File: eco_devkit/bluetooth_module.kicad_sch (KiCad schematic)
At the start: 0 parts

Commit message: Add bg22 symbol library and update symbol library table
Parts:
- added C1, C10, C12, C4, C6: 100nF, symbol Device:C
- added C11, C2, C3, C5: 1µF, symbol Device:C
- added C13: 1.3 pF, symbol Device:C
- added C14: 18 pF, symbol Device:C
- added C7: 1.2 pF, symbol Device:C
- added C8, C9: C, symbol Device:C
- added CDECOUPLE: 10µF, symbol Device:C
- added J1: Conn_Coaxial, symbol Connector:Conn_Coaxial
- added L1, L2: 47nH, symbol Device:L
- added L3: 2.6 nH, symbol Device:L
- added U1: ~, symbol bg22:bg22
- added Y1: 38.4 MHz, symbol Device:Crystal
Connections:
- new net: C10.1, C9.1, L1.1, U1.10 (RFVDD)
- new net: C13.1, C14.1, L3.2
- new net: C14.2, J1.1 (In)
- new net: C11.1, C12.1, L2.1, U1.13 (PAVDD)
- new net: CDECOUPLE.1, U1.24 (DECOUPLE)
- new net: C7.1, L3.1, U1.12 (RF2G4_IO)
- new net: U1.7 (HFXTAL_I), Y1.1
- new net: U1.8 (HFXTAL_O), Y1.2
- new net +3.3V: C1.1, C1.2, C10.2, C11.2, C12.2, C13.2, C2.1, C2.2, C3.1, C3.2, C4.1, C4.2, C5.1, C5.2, C6.1, C6.2, C7.2, C8.1, C8.2, C9.2, CDECOUPLE.2, J1.2 (Ext), L1.2, L2.2, U1.26 (VREGVDD), U1.27 (VREGVSS), U1.28 (DVDD), U1.29 (AVDD), U1.30 (IOVDD)
- no-connect marks 0 -> 1

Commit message: att mpn e fotoprint da bg22
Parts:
- U1: footprint (none) -> EFR32BG22C224F512GN32-C
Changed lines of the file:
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@@
 			)
 		)
-		(property "Footprint" ""
+		(property "Footprint" "EFR32BG22C224F512GN32-C"
 			(at 78.74 72.39 0)
 			(effects
@@
 			)
 		)
-		(property "Datasheet" ""
+		(property "Datasheet" "https://www.digikey.com.br/pt/products/detail/silicon-labs/EFR32BG22C224F512GN32-C/11610897"
 			(at 78.74 72.39 0)
 			(effects
@@
 			)
 		)
-		(property "Description" ""
+		(property "Description" "IC RF TXRX+MCU BLE 32QFN"
 			(at 78.74 72.39 0)
 			(effects

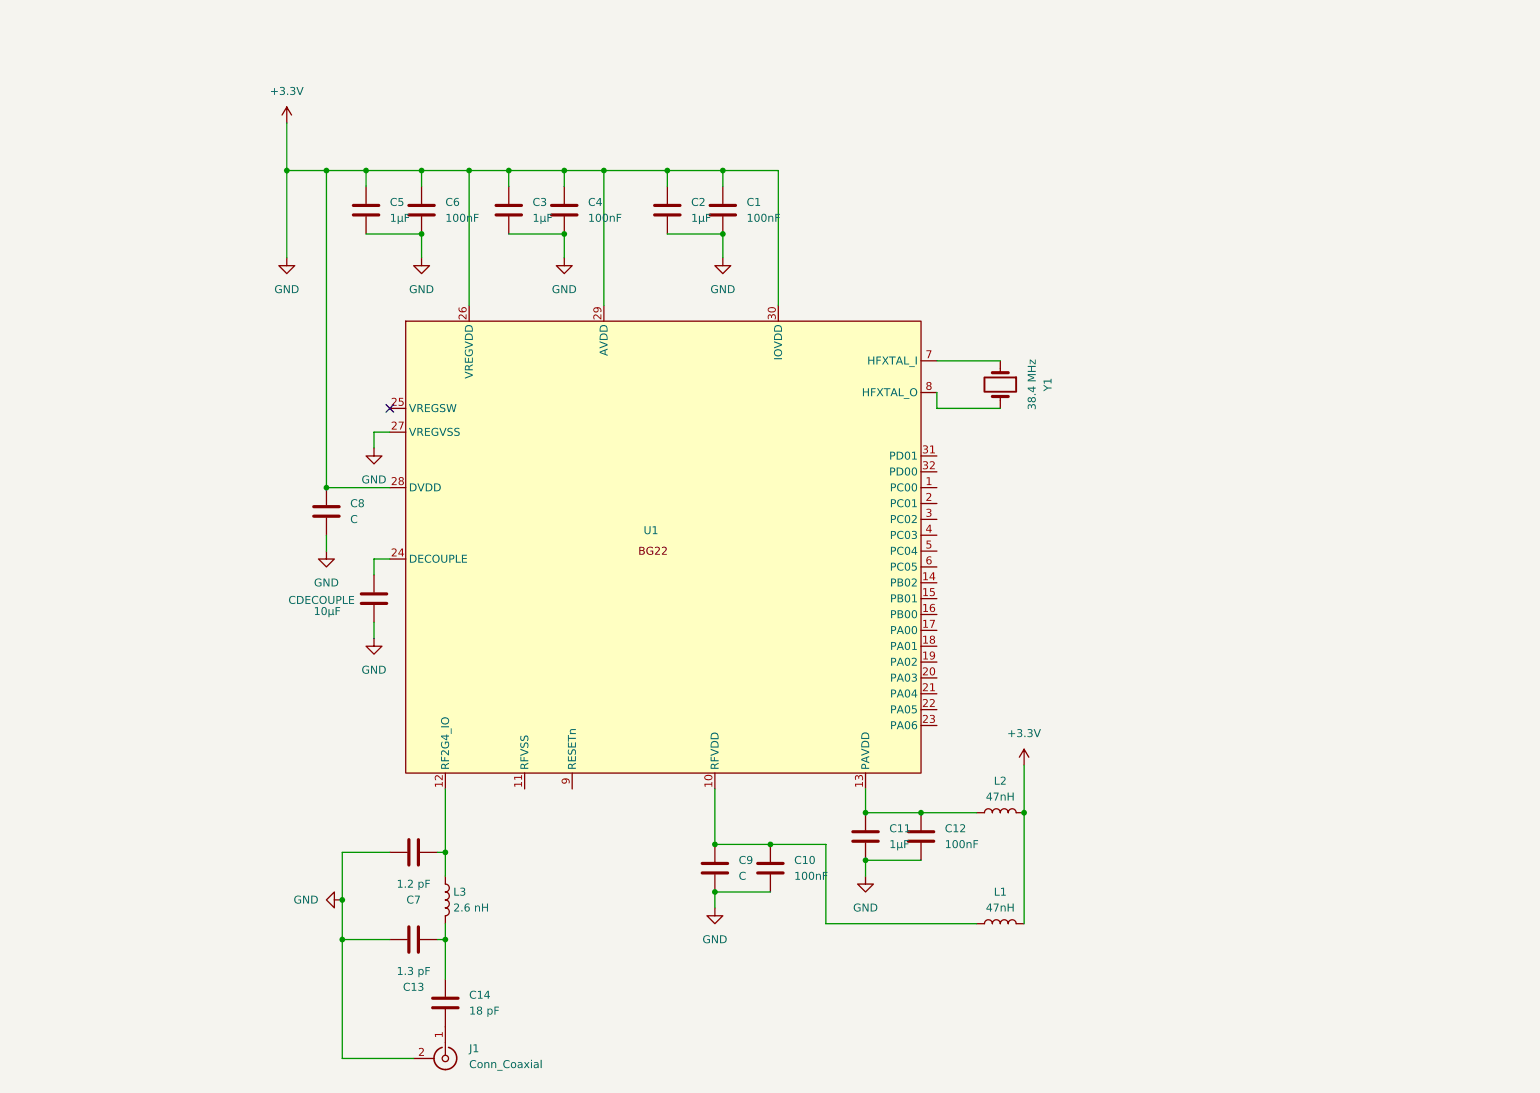
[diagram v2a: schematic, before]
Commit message: chore: ajustes nos periféricos GPIO e mapeamento do conector SWD
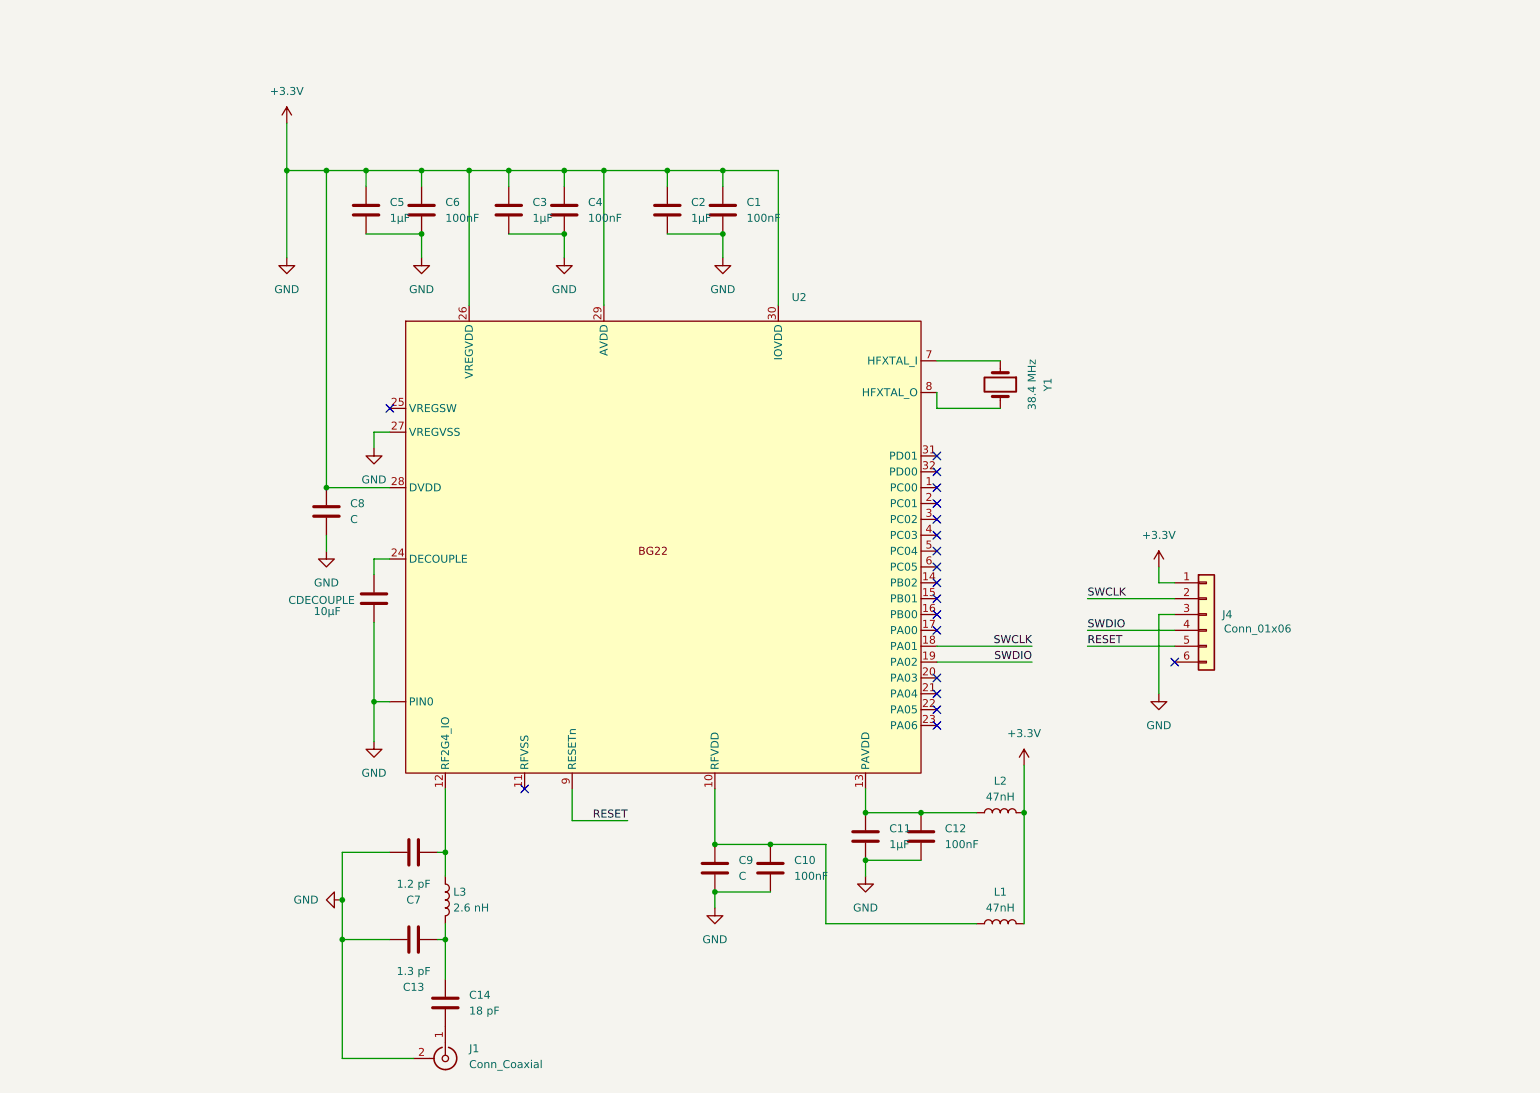
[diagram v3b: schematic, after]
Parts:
- removed U1: ~, EFR32BG22C224F512GN32-C, symbol bg22:bg22
- added J4: Conn_01x06, symbol Connector_Generic:Conn_01x06
- added U2: ~, EFR32BG22C224F512GN32-C, symbol bg22:bg22
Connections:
- net +3.3V: now also J4.1 (Pin_1), J4.3 (Pin_3), U2. (PIN0), U2.26 (VREGVDD), U2.27 (VREGVSS), U2.28 (DVDD), U2.29 (AVDD), U2.30 (IOVDD)
- net at C10.1, C9.1, L1.1: now also U2.10 (RFVDD)
- net at C11.1, C12.1, L2.1: now also U2.13 (PAVDD)
- net at CDECOUPLE.1: now also U2.24 (DECOUPLE)
- net at C7.1, L3.1: now also U2.12 (RF2G4_IO)
- net at Y1.1: now also U2.7 (HFXTAL_I)
- net at Y1.2: now also U2.8 (HFXTAL_O)
- new net RESET: J4.5 (Pin_5), U2.9 (RESETn)
- new net SWCLK: J4.2 (Pin_2), U2.18 (PA01)
- new net SWDIO: J4.4 (Pin_4), U2.19 (PA02)
- no-connect marks 1 -> 19

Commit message: Add bluetooth.
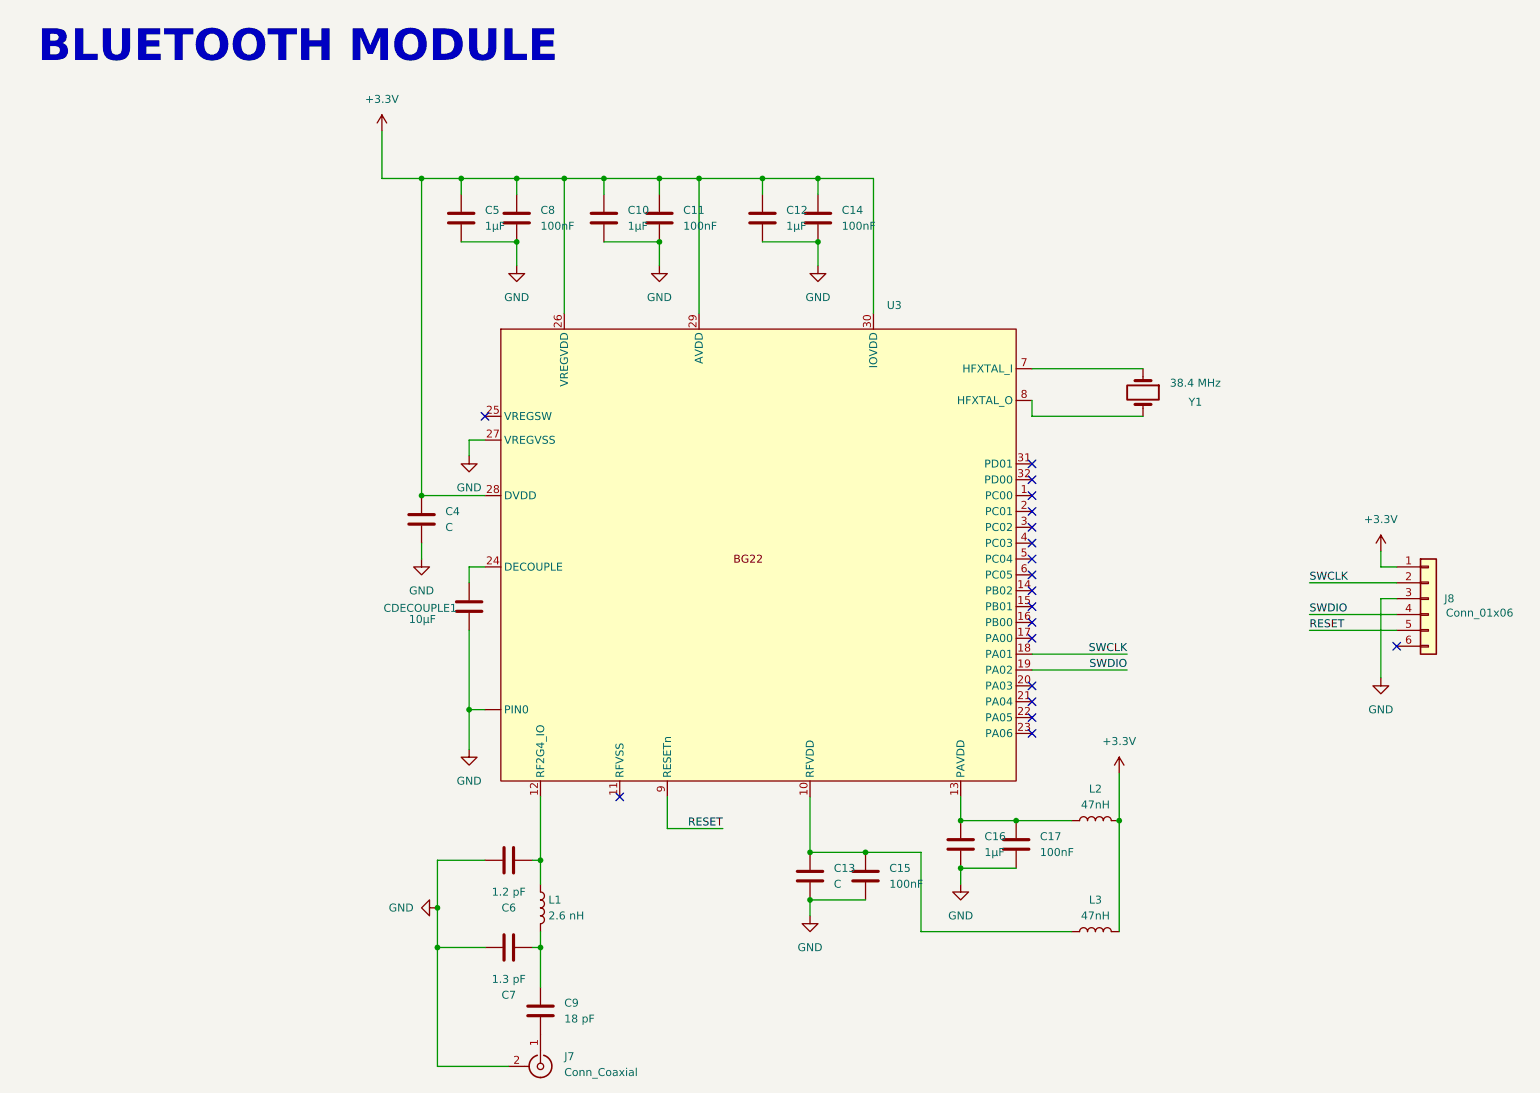
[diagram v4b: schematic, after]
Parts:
- J8: renamed from J4; footprint (none) -> Connector_PinHeader_2.54mm:PinHeader_1x06_P2.54mm_Vertical
- U3: renamed from U2; MPN (none) -> EFR32BG22C224F512GN32-C
- renumbered C3 to C10, C4 to C11, C2 to C12, C9 to C13, C1 to C14, C10 to C15, C11 to C16, C12 to C17, C8 to C4, C7 to C6, C13 to C7, C6 to C8, C14 to C9, CDECOUPLE to CDECOUPLE1, J1 to J7, L3 to L1, L1 to L3
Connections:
- net +3.3V: no longer C10.2, C11.2, C12.2, C13.2, C14.2, C15.2, C16.2, C17.2, C4.2, C5.2, C6.2, C7.2, C8.2, CDECOUPLE1.2, J7.2 (Ext), J8.3 (Pin_3), U3. (PIN0), U3.27 (VREGVSS)
- new net GND: C10.2, C11.2, C12.2, C13.2, C14.2, C15.2, C16.2, C17.2, C4.2, C5.2, C6.2, C7.2, C8.2, CDECOUPLE1.2, J7.2 (Ext), J8.3 (Pin_3), U3. (PIN0), U3.27 (VREGVSS)
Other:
- note added: "BLUETOOTH MODULE"
- moved on the sheet: C10, C11, C12, C13, C14, C15, C16, C17, C4, C5, C6, C7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

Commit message: First interation.
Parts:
- C25: renamed from C4; footprint (none) -> Capacitor_SMD:C_0402_1005Metric
- C26: renamed from C5; footprint (none) -> Capacitor_SMD:C_0402_1005Metric
- C27: renamed from C6; footprint (none) -> Capacitor_SMD:C_0402_1005Metric
- C28: renamed from C7; footprint (none) -> Capacitor_SMD:C_0402_1005Metric
- C29: renamed from C8; footprint (none) -> Capacitor_SMD:C_0402_1005Metric
- C30: renamed from C9; footprint (none) -> Capacitor_SMD:C_0402_1005Metric
- C31: renamed from C10; footprint (none) -> Capacitor_SMD:C_0402_1005Metric
- C32: renamed from C11; footprint (none) -> Capacitor_SMD:C_0402_1005Metric
- C33: renamed from C12; footprint (none) -> Capacitor_SMD:C_0402_1005Metric
- C34: renamed from C13; footprint (none) -> Capacitor_SMD:C_0402_1005Metric
- C35: renamed from C14; footprint (none) -> Capacitor_SMD:C_0402_1005Metric
- C36: renamed from C15; footprint (none) -> Capacitor_SMD:C_0402_1005Metric
- C37: renamed from C16; footprint (none) -> Capacitor_SMD:C_0402_1005Metric
- C38: renamed from C17; footprint (none) -> Capacitor_SMD:C_0402_1005Metric
- CDECOUPLE1: footprint (none) -> Capacitor_SMD:C_0402_1005Metric
- renumbered J8 to J10, J7 to J9, L1 to L2, L2 to L3, L3 to L4, Y1 to Y2
